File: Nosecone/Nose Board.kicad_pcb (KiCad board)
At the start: 2 copper layers, 45.7 x 63.5 mm, 55 parts, among them J1 Conn_01x02, J2 Conn_02x04_Odd_Even, J3 Conn_02x03_Odd_Even, J4 Conn_Coaxial, J5 Conn_01x02, Q1 Q_PMOS_DGS, Q2 Q_PMOS_DGS, U1 RS485_converter_ISL83488, U10 MS5803-14BA, U11 MS5803-14BA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

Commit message: Fixed via sizes, I think
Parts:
- renumbered U17 to ?
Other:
- board text added: "Daniel Corey Thomas Bennett"
- board text added: "UAH SHC Spaceport America Cup 2018 Nosecone avionics board"
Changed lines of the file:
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@@
     (links 172)
     (no_connects 79)
-    (area 134.544999 55.804999 180.415001 119.455001)
+    (area 124.46 43.18 195.580001 142.240001)
     (thickness 1.6)
-    (drawings 4)
-    (tracks 543)
+    (drawings 6)
+    (tracks 542)
     (zones 0)
     (modules 55)
@@
       (usegerberextensions false)
       (excludeedgelayer true)
-      (linewidth 0.100000)
+      (linewidth 0.128000)
       (plotframeref false)
       (viasonmask true)
@@
       (padsonsilk false)
       (subtractmaskfromsilk false)
-      (outputformat 4)
+      (outputformat 1)
       (mirror false)
-      (drillshape 2)
+      (drillshape 0)
       (scaleselection 1)
-      (outputdirectory PDFs/))
+      (outputdirectory "Generated Gerbers/Take4/"))
   )
   (net 0 "")
@@
   (module "Misc components:4_40_through_hole" (layer F.Cu)
     (at 138.303 113.157)
-    (fp_text reference U17 (at 0 0.5) (layer F.SilkS)
+    (fp_text reference "" (at 0 0.5) (layer F.SilkS)
       (effects (font (size 1 1) (thickness 0.15)))
     )
@@
     (pad 1 thru_hole circle (at 0 2.54) (size 3.25 3.25) (drill 2.95) (layers *.Cu *.Mask)
       (net 94 "Net-(U20-Pad1)"))
+  )
+  (gr_text "Daniel Corey\nThomas Bennett" (at 156.083 116.713) (layer F.SilkS)
+    (effects (font (size 1.5 1.5) (thickness 0.3)) (justify left))
+  )
+  (gr_text "UAH SHC Spaceport America Cup 2018\nNosecone avionics board" (at 157.353 113.665) (layer B.SilkS)
+    (effects (font (size 1.5 1.5) (thickness 0.3)) (justify mirror))
   )
   (gr_line (start 134.62 119.38) (end 134.62 55.88) (angle 90) (layer Edge.Cuts) (width 0.15))
@@
   (via (at 173.355 93.472) (size 0.6) (drill 0.4) (layers F.Cu B.Cu) (net 10))
   (segment (start 174.625 91.374) (end 174.625 93.515) (width 0.25) (layer F.Cu) (net 10))
+  (segment (start 160.315 77.79) (end 159.07 77.79) (width 0.25) (layer F.Cu) (net 11))
+  (segment (start 159.07 77.79) (end 156.185 74.905) (width 0.25) (layer F.Cu) (net 11))
+  (segment (start 156.185 74.905) (end 155.335 74.905) (width 0.25) (layer F.Cu) (net 11))
   (segment (start 176.175 110.236) (end 174.8255 108.8865) (width 0.25) (layer B.Cu) (net 11))
   (segment (start 178.7525 108.3945) (end 178.7525 109.691374) (width 0.25) (layer B.Cu) (net 11))
@@
   (segment (start 155.945 74.295) (end 157.48 74.295) (width 0.25) (layer F.Cu) (net 11))
   (via (at 157.48 74.295) (size 0.6) (drill 0.4) (layers F.Cu B.Cu) (net 11))
-  (segment (start 160.315 77.79) (end 159.705 77.79) (width 0.25) (layer F.Cu) (net 11))
-  (segment (start 159.705 77.79) (end 156.82 74.905) (width 0.25) (layer F.Cu) (net 11))
-  (segment (start 156.82 74.905) (end 155.335 74.905) (width 0.25) (layer F.Cu) (net 11))
   (segment (start 165.495 74.905) (end 165.495 75.49) (width 0.25) (layer F.Cu) (net 11))
   (segment (start 160.315 77.79) (end 162.565 77.79) (width 0.25) (layer F.Cu) (net 11))
@@
   (segment (start 175.8005 111.0865) (end 177.413 109.474) (width 0.25) (layer F.Cu) (net 20))
   (segment (start 175.4505 111.0865) (end 175.8005 111.0865) (width 0.25) (layer F.Cu) (net 20))
-  (segment (start 160.315 78.74) (end 158.115 78.74) (width 0.25) (layer F.Cu) (net 21))
-  (segment (start 154.965 76.835) (end 153.035 74.905) (width 0.25) (layer F.Cu) (net 21))
-  (segment (start 156.845 76.835) (end 154.965 76.835) (width 0.25) (layer F.Cu) (net 21))
-  (segment (start 157.48 77.47) (end 156.845 76.835) (width 0.25) (layer F.Cu) (net 21))
-  (segment (start 157.48 78.105) (end 157.48 77.47) (width 0.25) (layer F.Cu) (net 21))
-  (segment (start 158.115 78.74) (end 157.48 78.105) (width 0.25) (layer F.Cu) (net 21))
+  (segment (start 153.035 75.155) (end 153.035 74.905) (width 0.25) (layer F.Cu) (net 21))
+  (segment (start 156.902 76.327) (end 154.207 76.327) (width 0.25) (layer F.Cu) (net 21))
+  (segment (start 160.315 78.74) (end 159.315 78.74) (width 0.25) (layer F.Cu) (net 21))
+  (segment (start 154.207 76.327) (end 153.035 75.155) (width 0.25) (layer F.Cu) (net 21))
+  (segment (start 159.315 78.74) (end 156.902 76.327) (width 0.25) (layer F.Cu) (net 21))
   (segment (start 159.065 79.69) (end 158.877 79.502) (width 0.25) (layer F.Cu) (net 22))
   (segment (start 160.315 79.69) (end 159.065 79.69) (width 0.25) (layer F.Cu) (net 22))
@@
   (segment (start 139.7 72.74) (end 142.082 72.74) (width 0.25) (layer F.Cu) (net 39))
   (via (at 142.113 72.771) (size 0.6) (drill 0.4) (layers F.Cu B.Cu) (net 39))
-  (via (at 143.764 80.01) (size 0.6) (drill 0.4) (layers F.Cu B.Cu) (net 39))
+  (via (at 143.764 80.01) (size 0.6) (drill 0.3) (layers F.Cu B.Cu) (net 39))
   (segment (start 164.338 84.582) (end 160.909 84.582) (width 0.25) (layer F.Cu) (net 39))
   (via (at 160.909 84.582) (size 0.6) (drill 0.4) (layers F.Cu B.Cu) (net 39))
@@
   (segment (start 144.399 83.692998) (end 144.399002 83.693) (width 0.25) (layer B.Cu) (net 40))
   (segment (start 144.399 72.771) (end 144.399 83.692998) (width 0.25) (layer B.Cu) (net 40))
-  (via (at 144.399002 83.693) (size 0.6) (drill 0.4) (layers F.Cu B.Cu) (net 40))
+  (via (at 144.399002 83.693) (size 0.6) (drill 0.3) (layers F.Cu B.Cu) (net 40))
   (segment (start 159.404021 85.852) (end 159.739022 85.516999) (width 0.25) (layer B.Cu) (net 40))
   (segment (start 160.463285 85.217) (end 160.039021 85.217) (width 0.25) (layer F.Cu) (net 40))
@@
     (connect_pads (clearance 0.18))
     (min_thickness 0.18)
-    (fill (arc_segments 16) (thermal_gap 0.508) (thermal_bridge_width 0.508))
+    (fill yes (arc_segments 16) (thermal_gap 0.508) (thermal_bridge_width 0.508))
     (polygon
       (pts
@@
     (connect_pads (clearance 0.18))
     (min_thickness 0.18)
-    (fill (arc_segments 16) (thermal_gap 0.508) (thermal_bridge_width 0.508))
+    (fill yes (arc_segments 16) (thermal_gap 0.508) (thermal_bridge_width 0.508))
     (polygon
       (pts
@@
     (min_thickness 0.2)
     (keepout (tracks allowed) (vias allowed) (copperpour not_allowed))
-    (fill (arc_segments 16) (thermal_gap 0.508) (thermal_bridge_width 0.508))
+    (fill yes (arc_segments 16) (thermal_gap 0.508) (thermal_bridge_width 0.508))
     (polygon
       (pts

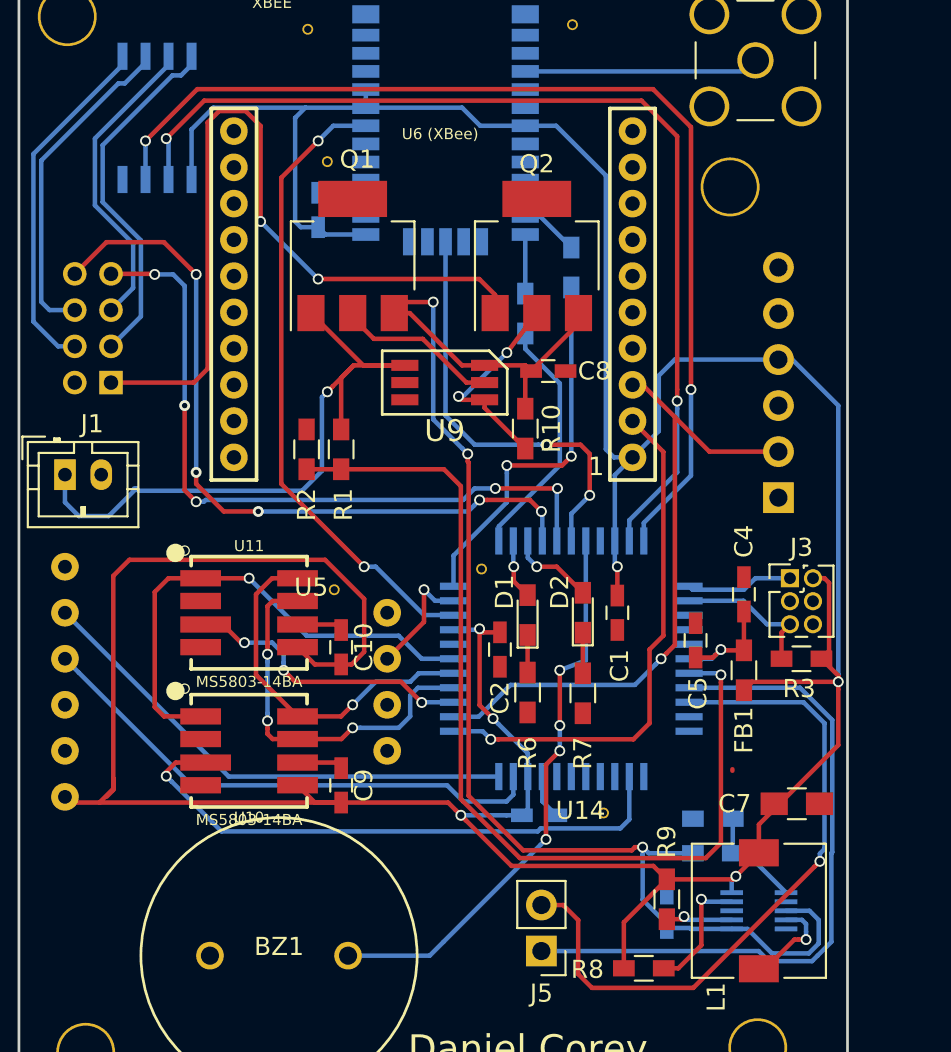
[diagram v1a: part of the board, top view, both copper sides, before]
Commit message: Actually fixed via sizes, I think
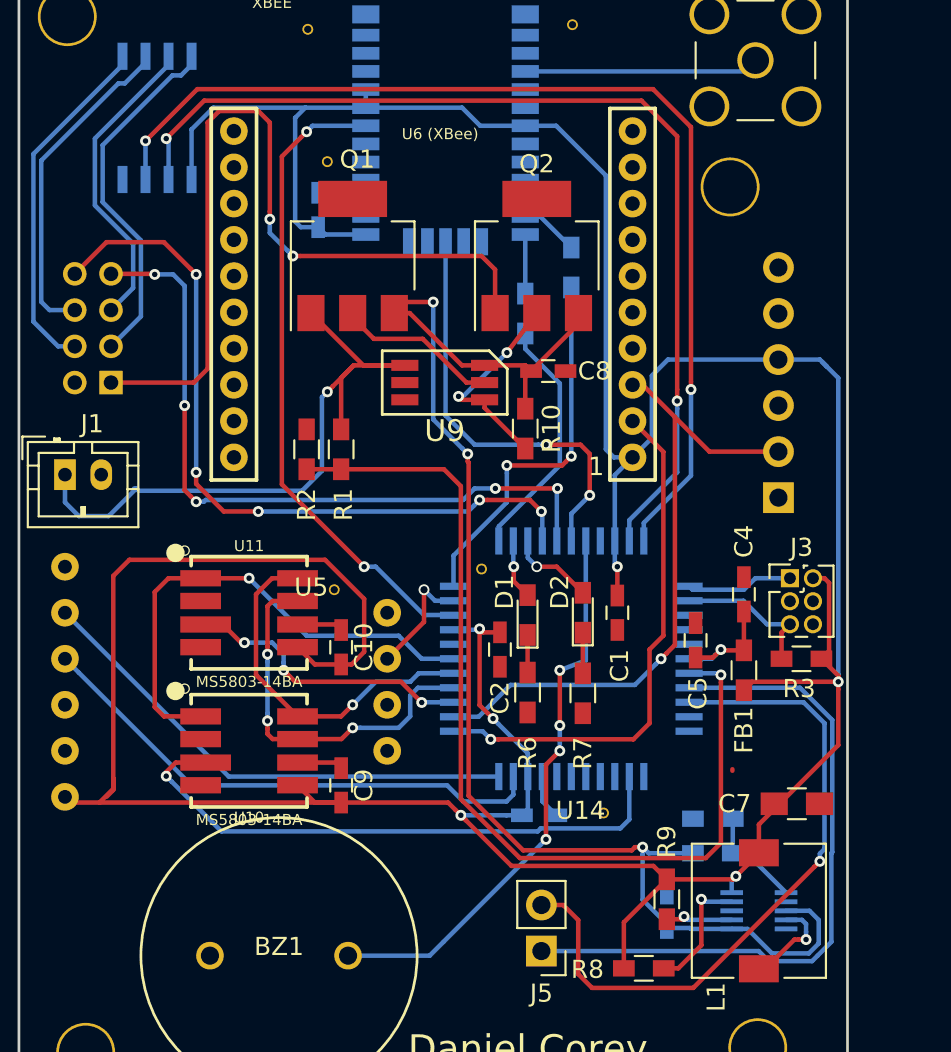
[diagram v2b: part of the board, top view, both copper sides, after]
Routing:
- net +3V3: track 223.8 -> 225.3 mm
- net VBUS: track 43.7 -> 45.0 mm
- net /GPS1_EXTINT: track 35.1 -> 35.7 mm
